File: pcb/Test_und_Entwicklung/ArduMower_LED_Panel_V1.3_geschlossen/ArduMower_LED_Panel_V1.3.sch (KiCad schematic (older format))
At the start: 32 parts, among them P1 Led Panel, P2 AnhebeS., P3 Button EX., P4 RES., P5 CONN_01X05, SW1 Button, SW2 SW_PUSH

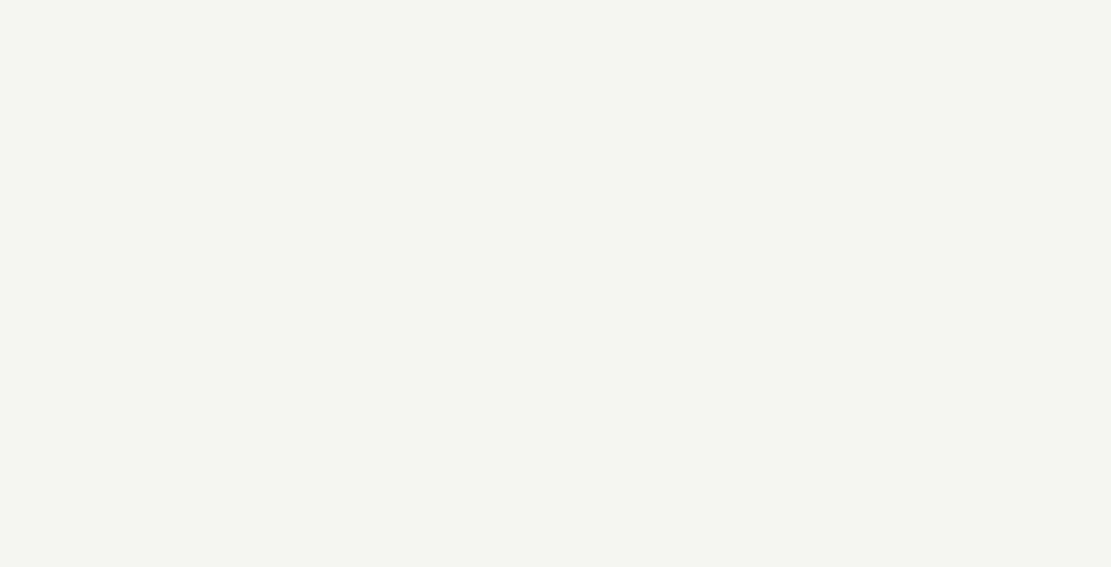
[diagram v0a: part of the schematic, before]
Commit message: ArduMower_LED_Panel_V1.3_geschlossen
ArduMower_LED_Panel_V1.3_geschlossen
Status von Platine von geöffnet auf geschlossen geändert.
Testplatine durch Jürgen kontrolliert
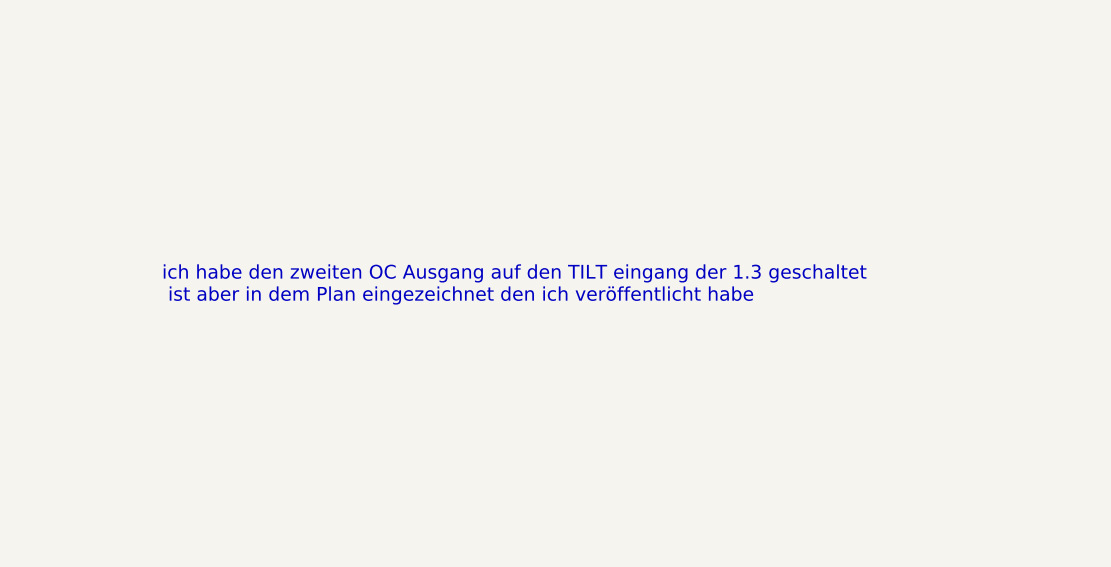
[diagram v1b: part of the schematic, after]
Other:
- note added: "ich habe den zweiten OC Ausgang auf den TILT eingang der 1.3 geschaltet\n ist aber in dem Plan eingezeichnet den ich veröffentlicht habe"
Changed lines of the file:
@@
 	1    0    0    -1
 $EndComp
+Text Notes 12310 3505 0    60   ~ 0
+ich habe den zweiten OC Ausgang auf den TILT eingang der 1.3 geschaltet\n ist aber in dem Plan eingezeichnet den ich veröffentlicht habe
 $EndSCHEMATC
